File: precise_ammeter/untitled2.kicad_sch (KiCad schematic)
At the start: 7 parts, among them U3 TLV9301xDBV

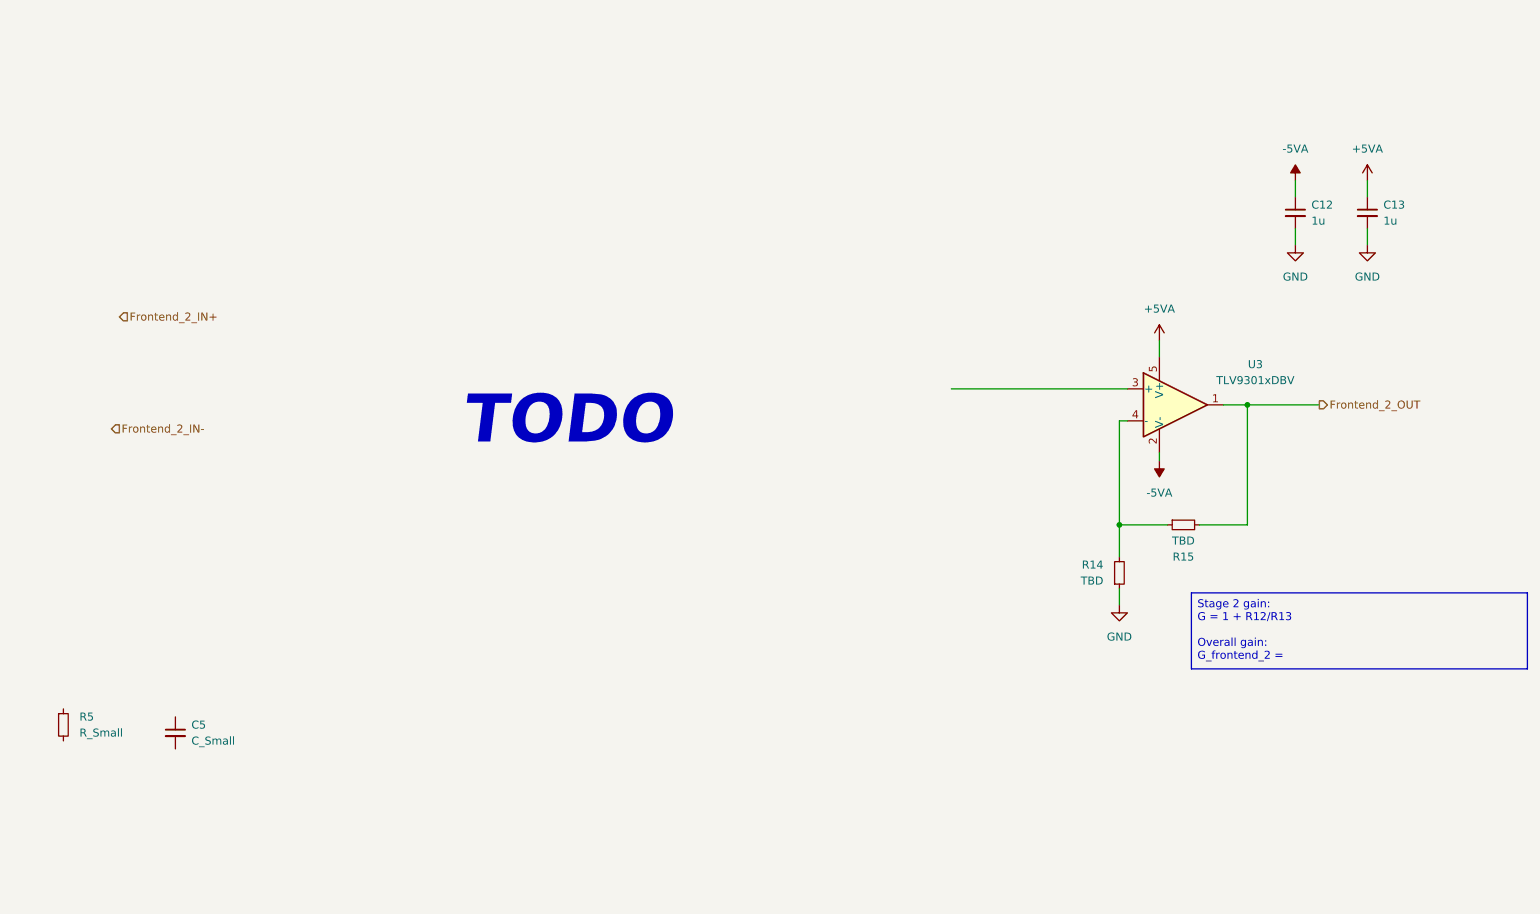
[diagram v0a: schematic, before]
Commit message: Dodano drugi schemat frontendu
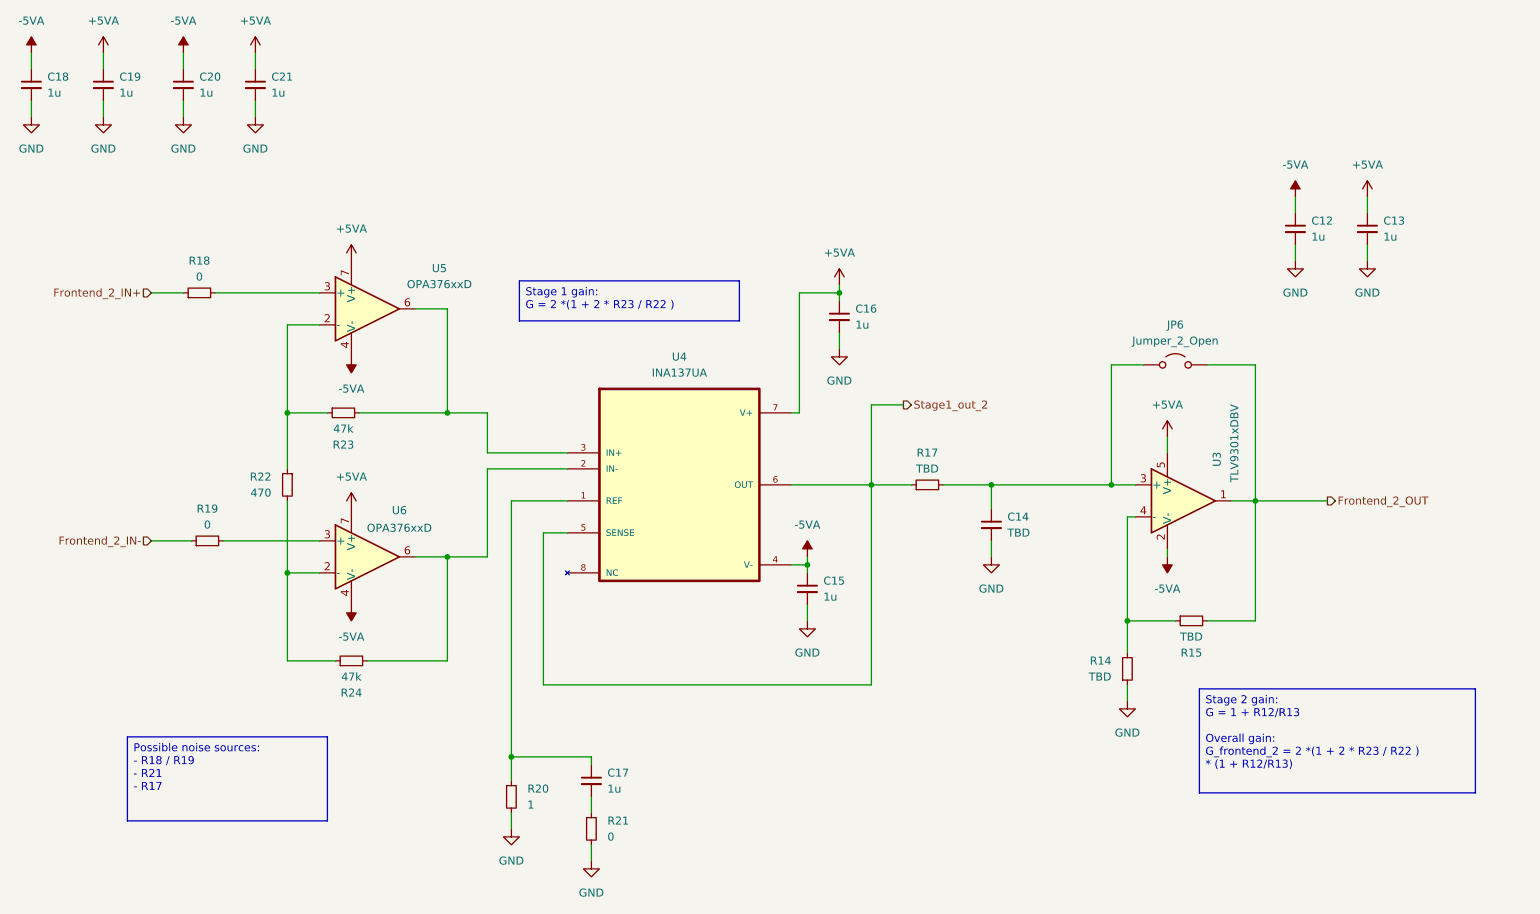
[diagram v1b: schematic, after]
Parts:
- removed C5: C_Small, Capacitor_SMD:C_0805_2012Metric_Pad1.18x1.45mm_HandSolder, symbol Device:C_Small
- removed R5: R_Small, Resistor_SMD:R_0805_2012Metric_Pad1.20x1.40mm_HandSolder, symbol Device:R_Small
- added C14: TBD, Capacitor_SMD:C_0805_2012Metric_Pad1.18x1.45mm_HandSolder, symbol Device:C_Small
- added C15, C16, C17, C18, C19, C20, C21: 1u, Capacitor_SMD:C_0805_2012Metric_Pad1.18x1.45mm_HandSolder, symbol Device:C_Small
- added JP6: Jumper_2_Open, symbol Jumper:Jumper_2_Open
- added R17: TBD, Resistor_SMD:R_0805_2012Metric_Pad1.20x1.40mm_HandSolder, symbol Device:R_Small
- added R18, R19, R21: 0, Resistor_SMD:R_0805_2012Metric_Pad1.20x1.40mm_HandSolder, symbol Device:R_Small
- added R20: 1, Resistor_SMD:R_0805_2012Metric_Pad1.20x1.40mm_HandSolder, symbol Device:R_Small
- added R22: 470, Resistor_SMD:R_0805_2012Metric_Pad1.20x1.40mm_HandSolder, symbol Device:R_Small
- added R23, R24: 47k, Resistor_SMD:R_0805_2012Metric_Pad1.20x1.40mm_HandSolder, symbol Device:R_Small
- added U4: INA137UA, INA137UA:SOIC127P599X175-8N, symbol INA137UA:INA137UA
- added U5, U6: OPA376xxD, Package_SO:SOIC-8_3.9x4.9mm_P1.27mm, symbol Amplifier_Operational:OPA376xxD
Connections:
- net +5VA: now also C16.1, C19.1, C21.1, U4.7 (V+), U5.7 (V+), U6.7 (V+)
- net -5VA: now also C15.1, C18.1, C20.1, U4.4 (V-), U5.4 (V-), U6.4 (V-)
- net Frontend_2_IN+: now also R18.1
- net Frontend_2_IN-: now also R19.1
- net Frontend_2_OUT: now also JP6.2 (B)
- net GND: now also C14.2, C15.2, C16.2, C18.2, C19.2, C20.2, C21.2, R20.2, R21.2
- net at U3.3 (+): now also C14.1, JP6.1 (A), R17.2
- new net: R22.2, R24.1, U6.2 (-)
- new net: R24.2, U4.2 (IN-), U6.6
- new net: R19.2, U6.3 (+)
- new net: R18.2, U5.3 (+)
- new net: C17.2, R21.1
- new net: C17.1, R20.1, U4.1 (REF)
- new net: R23.2, U4.3 (IN+), U5.6
- new net: R22.1, R23.1, U5.2 (-)
- new net Stage1_out_2: R17.1, U4.5 (SENSE), U4.6 (OUT)
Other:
- note removed: "TODO"
- moved on the sheet: C12, C13, R14, R15, U3

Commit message: dodano layout
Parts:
- JP6: footprint (none) -> Jumper:SolderJumper-2_P1.3mm_Open_Pad1.0x1.5mm
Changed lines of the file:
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@@
 			)
 		)
-		(property "Footprint" ""
+		(property "Footprint" "Jumper:SolderJumper-2_P1.3mm_Open_Pad1.0x1.5mm"
 			(at 212.09 82.55 0)
 			(effects

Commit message: unknown changes
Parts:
- R18, R19: value 0 -> 22k
- R22: value 470 -> 1.2k
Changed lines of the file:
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@@
 			)
 		)
-		(property "Value" "0"
+		(property "Value" "22k"
 			(at 58.42 107.95 90)
 			(effects
@@
 			)
 		)
-		(property "Value" "0"
+		(property "Value" "22k"
 			(at 57.15 68.58 90)
 			(effects
@@
 			)
 		)
-		(property "Value" "470"
+		(property "Value" "1.2k"
 			(at 68.58 102.8699 0)
 			(effects

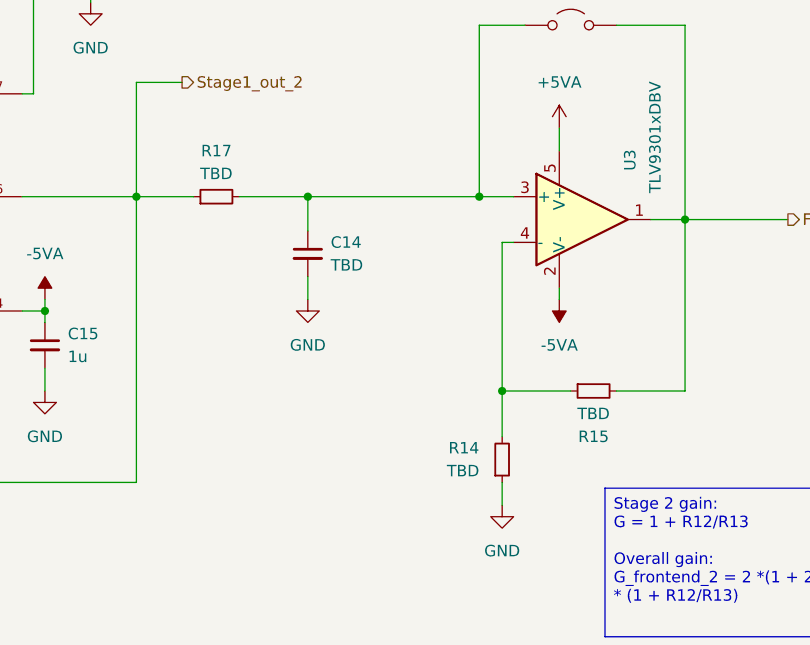
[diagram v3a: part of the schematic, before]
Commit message: added compoennt values for frontend 2
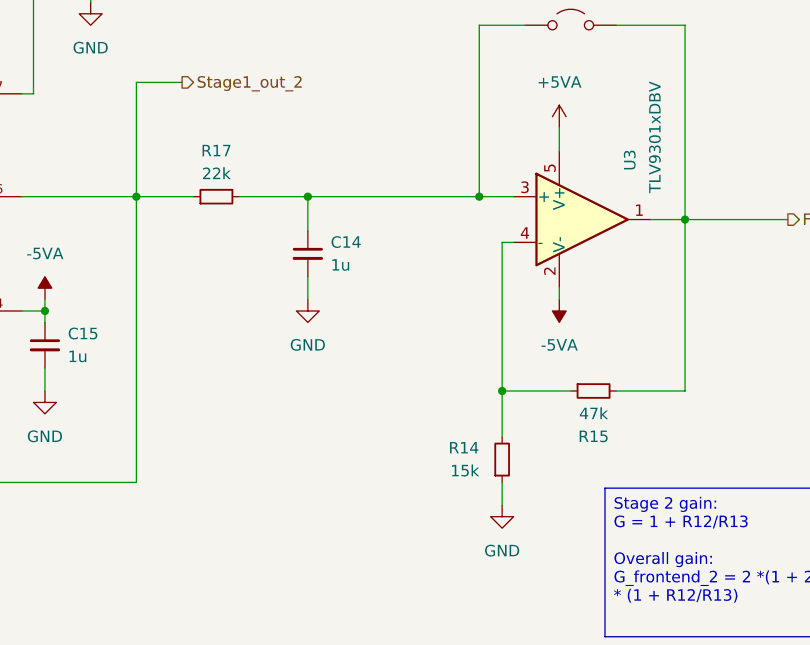
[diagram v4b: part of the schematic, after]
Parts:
- C14: value TBD -> 1u
- R14: value TBD -> 15k
- R15: value TBD -> 47k
- R17: value TBD -> 22k
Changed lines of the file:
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@@
 			)
 		)
-		(property "Value" "TBD"
+		(property "Value" "1u"
 			(at 185.42 109.2262 0)
 			(effects
@@
 			)
 		)
-		(property "Value" "TBD"
+		(property "Value" "22k"
 			(at 172.72 99.06 90)
 			(effects
@@
 			)
 		)
-		(property "Value" "TBD"
+		(property "Value" "47k"
 			(at 214.63 125.73 90)
 			(effects
@@
 			)
 		)
-		(property "Value" "TBD"
+		(property "Value" "15k"
 			(at 201.93 132.0799 0)
 			(effects
